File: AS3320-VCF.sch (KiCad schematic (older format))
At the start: 32 parts, among them J1 AudioJack2, J2 AudioJack2, J3 Conn_01x01_Male, J4 Conn_01x01_Male, J5 AudioJack2, U1 AS3320

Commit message: Replace board with new footprints for Audio Jacks and Potentiometers
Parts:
- removed J3, J4: Conn_01x01_Male, Connector_Pin:Pin_D1.0mm_L10.0mm, symbol Connector:Conn_01x01_Male
- removed R? (x2): 100K, symbol Device:R
- added R1: 330R, SeattleSynths:R_Axial_DIN0207_L6.3mm_D2.5mm_P10.16mm_Horizontal, symbol Device:R
- added R2: 72K, SeattleSynths:R_Axial_DIN0207_L6.3mm_D2.5mm_P10.16mm_Horizontal, symbol Device:R
- added R3, R7: 50K, SeattleSynths:R_Axial_DIN0207_L6.3mm_D2.5mm_P10.16mm_Horizontal, symbol Device:R
- added TP1: RES_CTRL, SeattleSynths:TestPoint_Pad_4.0x4.0mm, symbol Connector:TestPoint
- added TP2: +12V, SeattleSynths:TestPoint_Pad_4.0x4.0mm, symbol Connector:TestPoint
- added TP3: GND, SeattleSynths:TestPoint_Pad_4.0x4.0mm, symbol Connector:TestPoint
- added TP4: -12V, SeattleSynths:TestPoint_Pad_4.0x4.0mm, symbol Connector:TestPoint
- added TP5: FREQ_NTRL, SeattleSynths:TestPoint_Pad_4.0x4.0mm, symbol Connector:TestPoint
- added TP6: INPUT, SeattleSynths:TestPoint_Pad_4.0x4.0mm, symbol Connector:TestPoint
- added TP7: OUTPUT, SeattleSynths:TestPoint_Pad_4.0x4.0mm, symbol Connector:TestPoint
- C1, C2, C3, C4: footprint Capacitor_THT:CP_Radial_D5.0mm_P2.50mm -> SeattleSynths:C_Disc_D7.5mm_W2.5mm_P5.00mm
- C5: footprint Capacitor_THT:CP_Radial_D5.0mm_P2.50mm -> SeattleSynths:CP_Radial_D5.0mm_P2.50mm
- J1: renamed from J?; value AudioJack2 -> AUDIO INPUT; footprint Connector_Audio:Jack_6.35mm_Neutrik_NJ2FD-V_Vertical -> SeattleSynths:Jack_3.5mm_QingPu_WQP-PJ398SM_Vertical_CircularHoles
- J2: renamed from J1; value AudioJack2 -> RESONANCE CNTL. INPUT; footprint Connector_Audio:Jack_6.35mm_Neutrik_NJ2FD-V_Vertical -> SeattleSynths:Jack_3.5mm_QingPu_WQP-PJ398SM_Vertical_CircularHoles
- J3: renamed from J2; value AudioJack2 -> FREQ CNTL. INPUT; footprint Connector_Audio:Jack_6.35mm_Neutrik_NJ2FD-V_Vertical -> SeattleSynths:Jack_3.5mm_QingPu_WQP-PJ398SM_Vertical_CircularHoles
- J4: renamed from J5; value AudioJack2 -> AUDIO OUTPUT; footprint Connector_Audio:Jack_6.35mm_Neutrik_NJ2FD-V_Vertical -> SeattleSynths:Jack_3.5mm_QingPu_WQP-PJ398SM_Vertical_CircularHoles
- R10: renamed from R6; footprint Resistor_THT:R_Axial_DIN0207_L6.3mm_D2.5mm_P10.16mm_Horizontal -> SeattleSynths:R_Axial_DIN0207_L6.3mm_D2.5mm_P10.16mm_Horizontal
- R11: renamed from R7; footprint Resistor_THT:R_Axial_DIN0207_L6.3mm_D2.5mm_P10.16mm_Horizontal -> SeattleSynths:R_Axial_DIN0207_L6.3mm_D2.5mm_P10.16mm_Horizontal
- R12: renamed from R8; footprint Resistor_THT:R_Axial_DIN0207_L6.3mm_D2.5mm_P10.16mm_Horizontal -> SeattleSynths:R_Axial_DIN0207_L6.3mm_D2.5mm_P10.16mm_Horizontal
- R13: renamed from R9; footprint Resistor_THT:R_Axial_DIN0207_L6.3mm_D2.5mm_P10.16mm_Horizontal -> SeattleSynths:R_Axial_DIN0207_L6.3mm_D2.5mm_P10.16mm_Horizontal
- R14: renamed from R10; footprint Resistor_THT:R_Axial_DIN0207_L6.3mm_D2.5mm_P10.16mm_Horizontal -> SeattleSynths:R_Axial_DIN0207_L6.3mm_D2.5mm_P10.16mm_Horizontal
- R15: renamed from R11; footprint Resistor_THT:R_Axial_DIN0207_L6.3mm_D2.5mm_P10.16mm_Horizontal -> SeattleSynths:R_Axial_DIN0207_L6.3mm_D2.5mm_P10.16mm_Horizontal
- R16: renamed from R12; footprint Resistor_THT:R_Axial_DIN0207_L6.3mm_D2.5mm_P10.16mm_Horizontal -> SeattleSynths:R_Axial_DIN0207_L6.3mm_D2.5mm_P10.16mm_Horizontal
- R17: renamed from R13; footprint Resistor_THT:R_Axial_DIN0207_L6.3mm_D2.5mm_P10.16mm_Horizontal -> SeattleSynths:R_Axial_DIN0207_L6.3mm_D2.5mm_P10.16mm_Horizontal
- R18: renamed from R14; footprint Resistor_THT:R_Axial_DIN0207_L6.3mm_D2.5mm_P10.16mm_Horizontal -> SeattleSynths:R_Axial_DIN0207_L6.3mm_D2.5mm_P10.16mm_Horizontal
- R19: renamed from R15; footprint Resistor_THT:R_Axial_DIN0207_L6.3mm_D2.5mm_P10.16mm_Horizontal -> SeattleSynths:R_Axial_DIN0207_L6.3mm_D2.5mm_P10.16mm_Horizontal
- R20: renamed from R16; footprint Resistor_THT:R_Axial_DIN0207_L6.3mm_D2.5mm_P10.16mm_Horizontal -> SeattleSynths:R_Axial_DIN0207_L6.3mm_D2.5mm_P10.16mm_Horizontal
- R4: renamed from R3; footprint Resistor_THT:R_Axial_DIN0207_L6.3mm_D2.5mm_P10.16mm_Horizontal -> SeattleSynths:R_Axial_DIN0207_L6.3mm_D2.5mm_P10.16mm_Horizontal
- R5: renamed from R4; footprint Resistor_THT:R_Axial_DIN0207_L6.3mm_D2.5mm_P10.16mm_Horizontal -> SeattleSynths:R_Axial_DIN0207_L6.3mm_D2.5mm_P10.16mm_Horizontal
- R6: renamed from R5; footprint Resistor_THT:R_Axial_DIN0207_L6.3mm_D2.5mm_P10.16mm_Horizontal -> SeattleSynths:R_Axial_DIN0207_L6.3mm_D2.5mm_P10.16mm_Horizontal
- R8: renamed from R2; footprint Resistor_THT:R_Axial_DIN0207_L6.3mm_D2.5mm_P10.16mm_Horizontal -> SeattleSynths:R_Axial_DIN0207_L6.3mm_D2.5mm_P10.16mm_Horizontal
- R9: renamed from R1; footprint Resistor_THT:R_Axial_DIN0207_L6.3mm_D2.5mm_P10.16mm_Horizontal -> SeattleSynths:R_Axial_DIN0207_L6.3mm_D2.5mm_P10.16mm_Horizontal
- RV1, RV2: footprint Potentiometer_THT:Potentiometer_ACP_CA9-V10_Vertical -> SeattleSynths:Potentiometer_Alpha_RD901F-40-00D_Single_Vertical
- U1: footprint Package_DIP:DIP-18_W7.62mm -> SeattleSynths:DIP-18_W7.62mm
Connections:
- wire segments 82 -> 87
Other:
- moved on the sheet: R8, R9

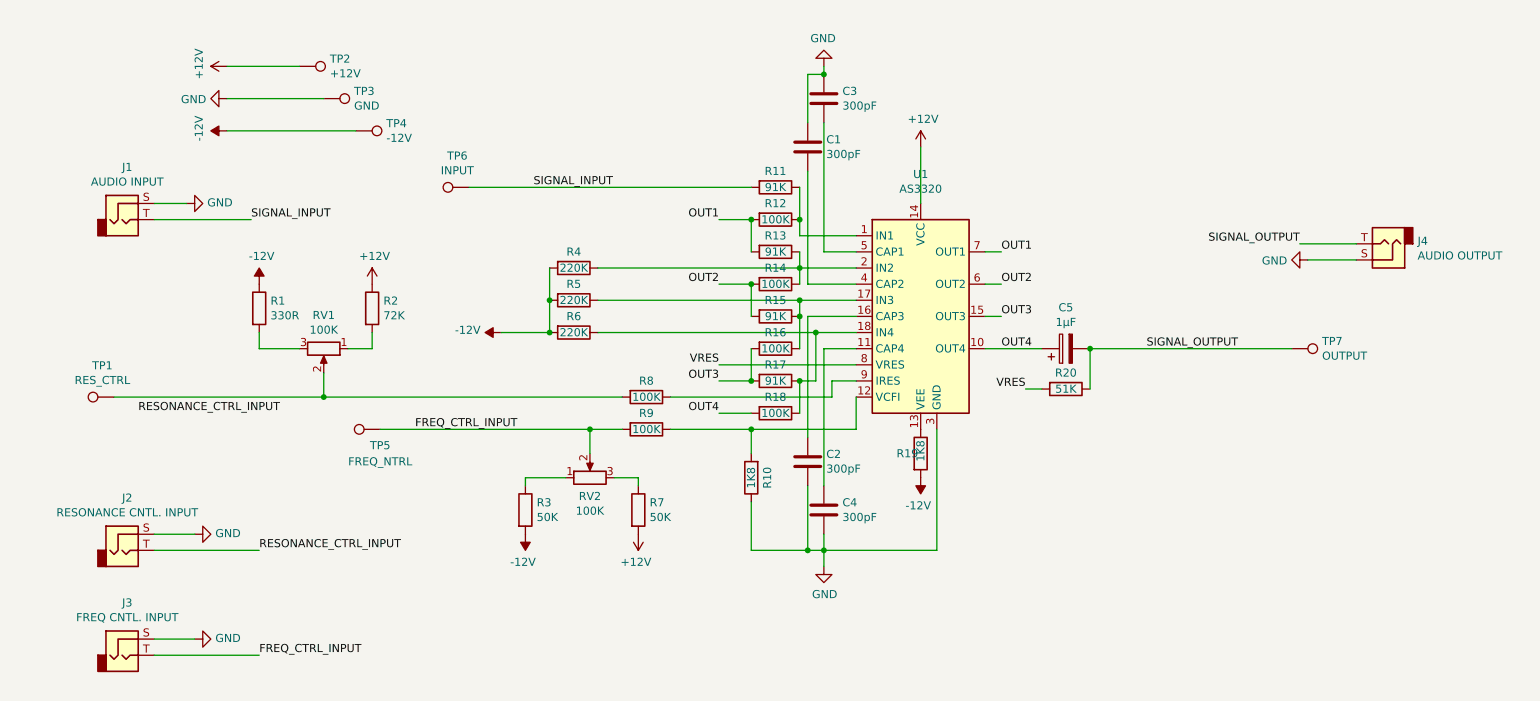
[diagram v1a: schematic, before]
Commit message: Replace board with new footprints for Audio Jacks and Potentiometers.
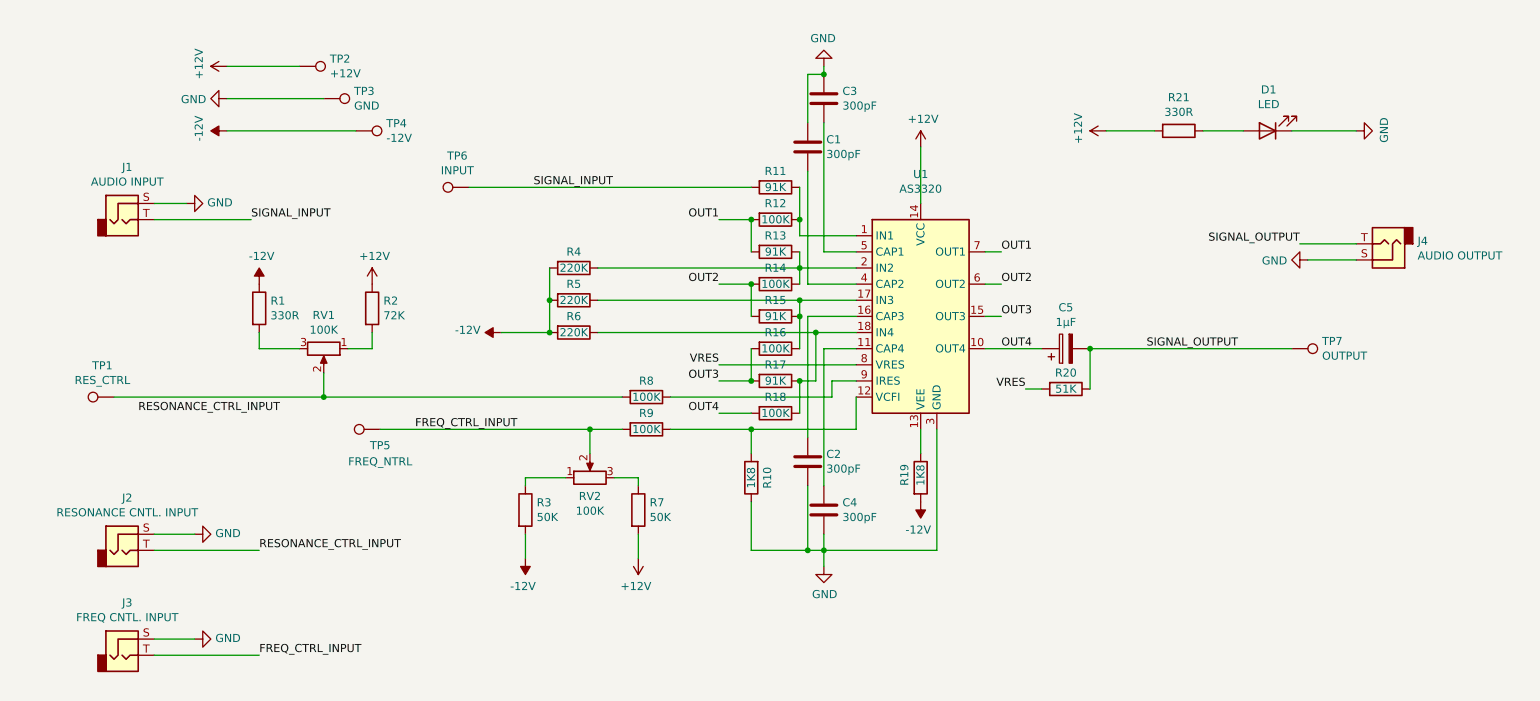
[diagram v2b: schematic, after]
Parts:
- added D1: LED, SeattleSynths:LED_D5.0mm, symbol Device:LED
- added R21: 330R, SeattleSynths:R_Axial_DIN0207_L6.3mm_D2.5mm_P10.16mm_Horizontal, symbol Device:R
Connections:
- net +12V: now also R21.2
- net GND: now also D1.1 (K)
- new net: D1.2 (A), R21.1
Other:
- moved on the sheet: R19
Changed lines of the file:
@@
 Text Label 2350 5200 0    50   ~ 0
 RESONANCE_CTRL_INPUT
-$Comp
-L power:-12V #PWR015
-U 1 1 5F9E2588
-P 6450 4750
-F 0 "#PWR015" H 6450 4850 50  0001 C CNN
-F 1 "-12V" H 6465 4923 50  0000 C CNN
-F 2 "" H 6450 4750 50  0001 C CNN
-F 3 "" H 6450 4750 50  0001 C CNN
-	1    6450 4750
-	-1   0    0    1
-$EndComp
 Wire Wire Line
 	6050 4150 5900 4150
@@
 Wire Wire Line
 	6450 3050 6450 2700
-$Comp
-L Device:R R19
-U 1 1 5F7C0487
-P 6450 4600
-F 0 "R19" H 6300 4600 50  0000 L CNN
-F 1 "1K8" V 6450 4550 50  0000 L CNN
-F 2 "SeattleSynths:R_Axial_DIN0207_L6.3mm_D2.5mm_P10.16mm_Horizontal" V 6380 4600 50  0001 C CNN
-F 3 "~" H 6450 4600 50  0001 C CNN
-	1    6450 4600
-	1    0    0    -1
-$EndComp
 Wire Wire Line
 	6050 4250 6050 4450
@@
 L power:-12V #PWR010
 U 1 1 5F8B473C
-P 4000 5100
-F 0 "#PWR010" H 4000 5200 50  0001 C CNN
-F 1 "-12V" H 4015 5273 50  0000 C CNN
-F 2 "" H 4000 5100 50  0001 C CNN
-F 3 "" H 4000 5100 50  0001 C CNN
-	1    4000 5100
+P 4000 5250
+F 0 "#PWR010" H 4000 5350 50  0001 C CNN
+F 1 "-12V" H 4015 5423 50  0000 C CNN
+F 2 "" H 4000 5250 50  0001 C CNN
+F 3 "" H 4000 5250 50  0001 C CNN
+	1    4000 5250
 	-1   0    0    1
 $EndComp
@@
 L power:+12V #PWR011
 U 1 1 5F8B55F7
-P 4700 5100
-F 0 "#PWR011" H 4700 4950 50  0001 C CNN
-F 1 "+12V" H 4715 5273 50  0000 C CNN
-F 2 "" H 4700 5100 50  0001 C CNN
-F 3 "" H 4700 5100 50  0001 C CNN
-	1    4700 5100
+P 4700 5250
+F 0 "#PWR011" H 4700 5100 50  0001 C CNN
+F 1 "+12V" H 4715 5423 50  0000 C CNN
+F 2 "" H 4700 5250 50  0001 C CNN
+F 3 "" H 4700 5250 50  0001 C CNN
+	1    4700 5250
 	-1   0    0    1
 $EndComp
@@
 	1    0    0    -1
 $EndComp
+$Comp
+L Device:LED D1
+U 1 1 5F9C1F74
+P 8600 2600
+F 0 "D1" H 8593 2345 50  0000 C CNN
+F 1 "LED" H 8593 2436 50  0000 C CNN
+F 2 "SeattleSynths:LED_D5.0mm" H 8600 2600 50  0001 C CNN
+F 3 "~" H 8600 2600 50  0001 C CNN
+	1    8600 2600
+	-1   0    0    1
+$EndComp
+$Comp
+L power:+12V #PWR0101
+U 1 1 5F9C478A
+P 7600 2600
+F 0 "#PWR0101" H 7600 2450 50  0001 C CNN
+F 1 "+12V" H 7615 2773 50  0000 C CNN
+F 2 "" H 7600 2600 50  0001 C CNN
+F 3 "" H 7600 2600 50  0001 C CNN
+	1    7600 2600
+	0    -1   -1   0
+$EndComp
+$Comp
+L Device:R R21
+U 1 1 5F9C722A
+P 8050 2600
+F 0 "R21" V 7843 2600 50  0000 C CNN
+F 1 "330R" V 7934 2600 50  0000 C CNN
+F 2 "SeattleSynths:R_Axial_DIN0207_L6.3mm_D2.5mm_P10.16mm_Horizontal" V 7980 2600 50  0001 C CNN
+F 3 "~" H 8050 2600 50  0001 C CNN
+	1    8050 2600
+	0    1    1    0
+$EndComp
+Wire Wire Line
+	7600 2600 7900 2600
+Wire Wire Line
+	8200 2600 8450 2600
+$Comp
+L power:GND #PWR0102
+U 1 1 5F9D4349
+P 9150 2600
+F 0 "#PWR0102" H 9150 2350 50  0001 C CNN
+F 1 "GND" H 9155 2427 50  0000 C CNN
+F 2 "" H 9150 2600 50  0001 C CNN
+F 3 "" H 9150 2600 50  0001 C CNN
+	1    9150 2600
+	0    -1   -1   0
+$EndComp
+Wire Wire Line
+	9150 2600 8750 2600
+$Comp
+L Device:R R19
+U 1 1 5F7C0487
+P 6450 4750
+F 0 "R19" V 6350 4700 50  0000 L CNN
+F 1 "1K8" V 6450 4700 50  0000 L CNN
+F 2 "SeattleSynths:R_Axial_DIN0207_L6.3mm_D2.5mm_P10.16mm_Horizontal" V 6380 4750 50  0001 C CNN
+F 3 "~" H 6450 4750 50  0001 C CNN
+	1    6450 4750
+	1    0    0    -1
+$EndComp
+$Comp
+L power:-12V #PWR015
+U 1 1 5F9E2588
+P 6450 4900
+F 0 "#PWR015" H 6450 5000 50  0001 C CNN
+F 1 "-12V" H 6465 5073 50  0000 C CNN
+F 2 "" H 6450 4900 50  0001 C CNN
+F 3 "" H 6450 4900 50  0001 C CNN
+	1    6450 4900
+	-1   0    0    1
+$EndComp
+Wire Wire Line
+	6450 4450 6450 4600
+Wire Wire Line
+	4000 5250 4000 5100
+Wire Wire Line
+	4700 5250 4700 5100
 $EndSCHEMATC

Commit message: Fix ERC errors.
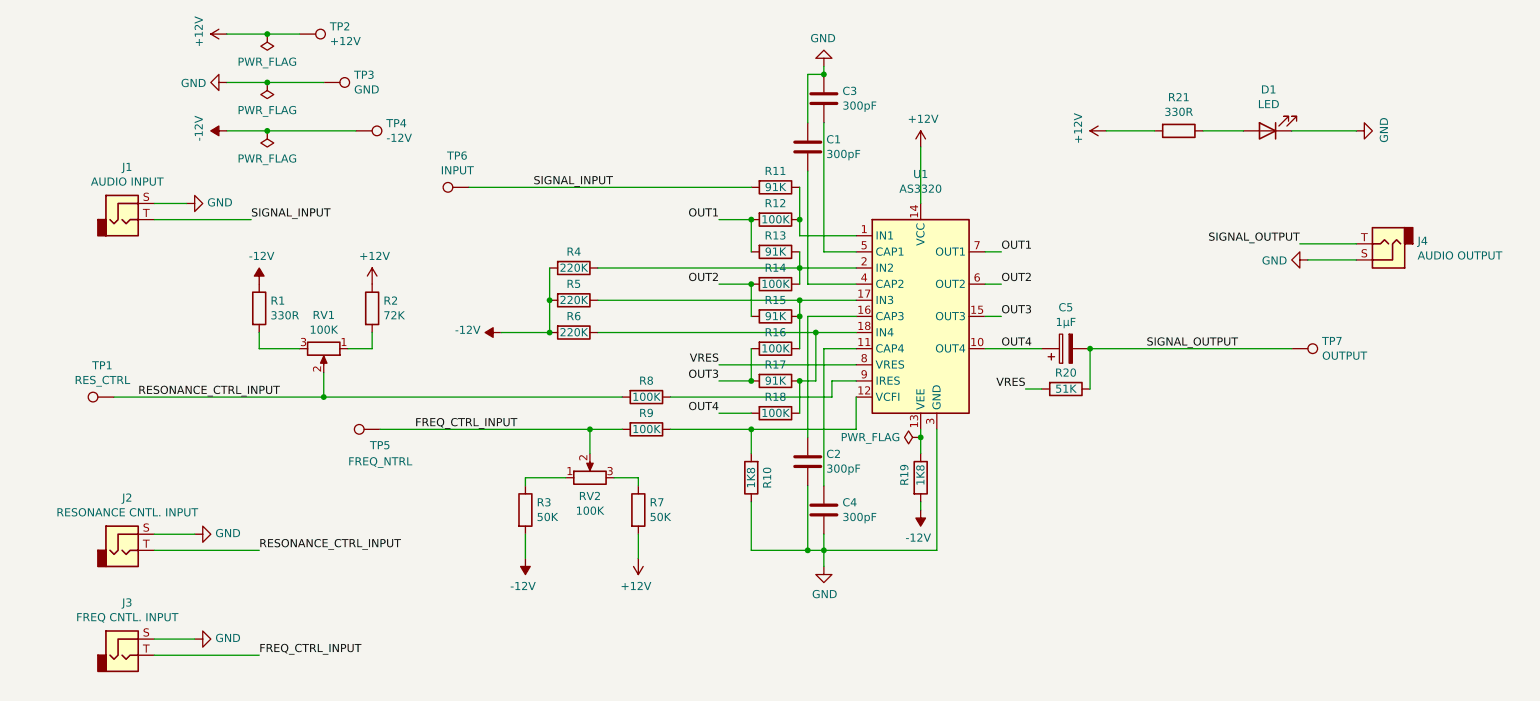
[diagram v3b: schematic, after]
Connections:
- net RESONANCE_CTRL_INPUT: now also R8.2, RV1.2, TP1.1
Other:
- moved on the sheet: TP2, TP3

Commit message: Refactor to use switched audio jacks.
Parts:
- removed J1: AUDIO INPUT, SeattleSynths:Jack_3.5mm_QingPu_WQP-PJ398SM_Vertical_CircularHoles, symbol Connector:AudioJack2
- removed J2: RESONANCE CNTL. INPUT, SeattleSynths:Jack_3.5mm_QingPu_WQP-PJ398SM_Vertical_CircularHoles, symbol Connector:AudioJack2
- removed J3: FREQ CNTL. INPUT, SeattleSynths:Jack_3.5mm_QingPu_WQP-PJ398SM_Vertical_CircularHoles, symbol Connector:AudioJack2
- removed J4: AUDIO OUTPUT, SeattleSynths:Jack_3.5mm_QingPu_WQP-PJ398SM_Vertical_CircularHoles, symbol Connector:AudioJack2
- added J5: SIGNAL_INPUT, SeattleSynths:Jack_3.5mm_QingPu_WQP-PJ398SM_Vertical_CircularHoles, symbol Connector:AudioJack2_SwitchT
- added J?: RESONANCE_CTRL_INPUT, SeattleSynths:Jack_3.5mm_QingPu_WQP-PJ398SM_Vertical_CircularHoles, symbol Connector:AudioJack2_SwitchT
- added J?: FREQ_CTRL_INPUT, SeattleSynths:Jack_3.5mm_QingPu_WQP-PJ398SM_Vertical_CircularHoles, symbol Connector:AudioJack2_SwitchT
- added J?: SIGNAL_OUTPUT, SeattleSynths:Jack_3.5mm_QingPu_WQP-PJ398SM_Vertical_CircularHoles, symbol Connector:AudioJack2_SwitchT
- TP5: value FREQ_NTRL -> FREQ_CTRL
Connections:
- net FREQ_CTRL_INPUT: now also J?.T
- net GND: now also J5.S, J?.S, J?.S, J?.S
- net RESONANCE_CTRL_INPUT: now also J?.T
- net SIGNAL_INPUT: now also J5.T
- net SIGNAL_OUTPUT: now also J?.T
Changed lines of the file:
@@
 	0    -1   -1   0
-$EndComp
-$Comp
-L Connector:AudioJack2 J3
-U 1 1 5F80A601
-P 1500 5850
-F 0 "J3" H 1532 6175 50  0000 C CNN
-F 1 "FREQ CNTL. INPUT" H 1532 6084 50  0000 C CNN
-F 2 "SeattleSynths:Jack_3.5mm_QingPu_WQP-PJ398SM_Vertical_CircularHoles" H 1500 5850 50  0001 C CNN
-F 3 "~" H 1500 5850 50  0001 C CNN
-	1    1500 5850
-	1    0    0    -1
-$EndComp
-$Comp
-L Connector:AudioJack2 J4
-U 1 1 5F808990
-P 9350 3300
-F 0 "J4" H 9170 3283 50  0000 R CNN
-F 1 "AUDIO OUTPUT" H 9170 3374 50  0000 R CNN
-F 2 "SeattleSynths:Jack_3.5mm_QingPu_WQP-PJ398SM_Vertical_CircularHoles" H 9350 3300 50  0001 C CNN
-F 3 "~" H 9350 3300 50  0001 C CNN
-	1    9350 3300
-	-1   0    0    1
 $EndComp
 Text Label 7100 4200 2    50   ~ 0
@@
 	5850 3950 5850 4800
 $Comp
-L Connector:AudioJack2 J1
-U 1 1 5F78D8C8
-P 1500 3150
-F 0 "J1" H 1532 3475 50  0000 C CNN
-F 1 "AUDIO INPUT" H 1532 3384 50  0000 C CNN
-F 2 "SeattleSynths:Jack_3.5mm_QingPu_WQP-PJ398SM_Vertical_CircularHoles" H 1500 3150 50  0001 C CNN
-F 3 "~" H 1500 3150 50  0001 C CNN
-	1    1500 3150
-	1    0    0    -1
-$EndComp
-$Comp
 L power:GND #PWR02
 U 1 1 5F81E5DD
@@
 Wire Wire Line
 	1700 5100 1950 5100
-$Comp
-L Connector:AudioJack2 J2
-U 1 1 5F80937B
-P 1500 5200
-F 0 "J2" H 1532 5525 50  0000 C CNN
-F 1 "RESONANCE CNTL. INPUT" H 1532 5434 50  0000 C CNN
-F 2 "SeattleSynths:Jack_3.5mm_QingPu_WQP-PJ398SM_Vertical_CircularHoles" H 1500 5200 50  0001 C CNN
-F 3 "~" H 1500 5200 50  0001 C CNN
-	1    1500 5200
-	1    0    0    -1
-$EndComp
 Text Label 4050 2950 0    50   ~ 0
 SIGNAL_INPUT
@@
 L power:GND #PWR01
 U 1 1 5F7AF0DD
-P 1900 3050
-F 0 "#PWR01" H 1900 2800 50  0001 C CNN
-F 1 "GND" V 1905 2922 50  0000 R CNN
-F 2 "" H 1900 3050 50  0001 C CNN
-F 3 "" H 1900 3050 50  0001 C CNN
-	1    1900 3050
-	0    -1   -1   0
-$EndComp
-Wire Wire Line
-	1700 3050 1900 3050
-Wire Wire Line
-	1700 3150 2300 3150
-Text Label 2300 3150 0    50   ~ 0
-SIGNAL_INPUT
+P 1450 3050
+F 0 "#PWR01" H 1450 2800 50  0001 C CNN
+F 1 "GND" V 1455 2922 50  0000 R CNN
+F 2 "" H 1450 3050 50  0001 C CNN
+F 3 "" H 1450 3050 50  0001 C CNN
+	1    1450 3050
+	0    -1   -1   0
+$EndComp
 Wire Wire Line
 	3650 2950 5400 2950
@@
 P 3100 4450
 F 0 "TP5" V 3000 4450 50  0000 C CNN
-F 1 "FREQ_NTRL" V 2900 4450 50  0000 C CNN
+F 1 "FREQ_CTRL" V 2900 4450 50  0000 C CNN
 F 2 "SeattleSynths:TestPoint_Pad_4.0x4.0mm" H 3300 4450 50  0001 C CNN
 F 3 "~" H 3300 4450 50  0001 C CNN
@@
 Wire Wire Line
 	6450 4500 6450 4600
+$Comp
+L Connector:AudioJack2_SwitchT J5
+U 1 1 5F9F3358
+P 1100 3150
+F 0 "J5" H 1132 3475 50  0000 C CNN
+F 1 "SIGNAL_INPUT" H 1132 3384 50  0000 C CNN
+F 2 "SeattleSynths:Jack_3.5mm_QingPu_WQP-PJ398SM_Vertical_CircularHoles" H 1100 3150 50  0001 C CNN
+F 3 "~" H 1100 3150 50  0001 C CNN
+	1    1100 3150
+	1    0    0    -1
+$EndComp
+Wire Wire Line
+	1450 3050 1300 3050
+Wire Wire Line
+	1300 3150 1850 3150
+Text Label 1850 3150 0    50   ~ 0
+SIGNAL_INPUT
+$Comp
+L Connector:AudioJack2_SwitchT J?
+U 1 1 5FA3B8F2
+P 1500 5200
+F 0 "J?" H 1532 5525 50  0000 C CNN
+F 1 "RESONANCE_CTRL_INPUT" H 1532 5434 50  0000 C CNN
+F 2 "SeattleSynths:Jack_3.5mm_QingPu_WQP-PJ398SM_Vertical_CircularHoles" H 1500 5200 50  0001 C CNN
+F 3 "~" H 1500 5200 50  0001 C CNN
+	1    1500 5200
+	1    0    0    -1
+$EndComp
+$Comp
+L Connector:AudioJack2_SwitchT J?
+U 1 1 5FA4A748
+P 1500 5850
+F 0 "J?" H 1532 6175 50  0000 C CNN
+F 1 "FREQ_CTRL_INPUT" H 1532 6084 50  0000 C CNN
+F 2 "SeattleSynths:Jack_3.5mm_QingPu_WQP-PJ398SM_Vertical_CircularHoles" H 1500 5850 50  0001 C CNN
+F 3 "~" H 1500 5850 50  0001 C CNN
+	1    1500 5850
+	1    0    0    -1
+$EndComp
+$Comp
+L Connector:AudioJack2_SwitchT J?
+U 1 1 5FA52FF0
+P 9350 3300
+F 0 "J?" H 9170 3233 50  0000 R CNN
+F 1 "SIGNAL_OUTPUT" H 9170 3324 50  0000 R CNN
+F 2 "SeattleSynths:Jack_3.5mm_QingPu_WQP-PJ398SM_Vertical_CircularHoles" H 9350 3300 50  0001 C CNN
+F 3 "~" H 9350 3300 50  0001 C CNN
+	1    9350 3300
+	-1   0    0    1
+$EndComp
 $EndSCHEMATC
